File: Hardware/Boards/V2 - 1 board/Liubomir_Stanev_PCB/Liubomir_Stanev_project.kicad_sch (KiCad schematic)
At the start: 16 parts, among them J2 Conn_01x03_Pin, J3 Conn_01x02_Pin, J6 Conn_01x02_Pin, U2 DS18B20-air, U2 DS18B20-water, U4 TEMT6000, U4 Turbidity sensor, U5 GY-8511 UV sensor, U6 Water Level Sensor, U7 ESP32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

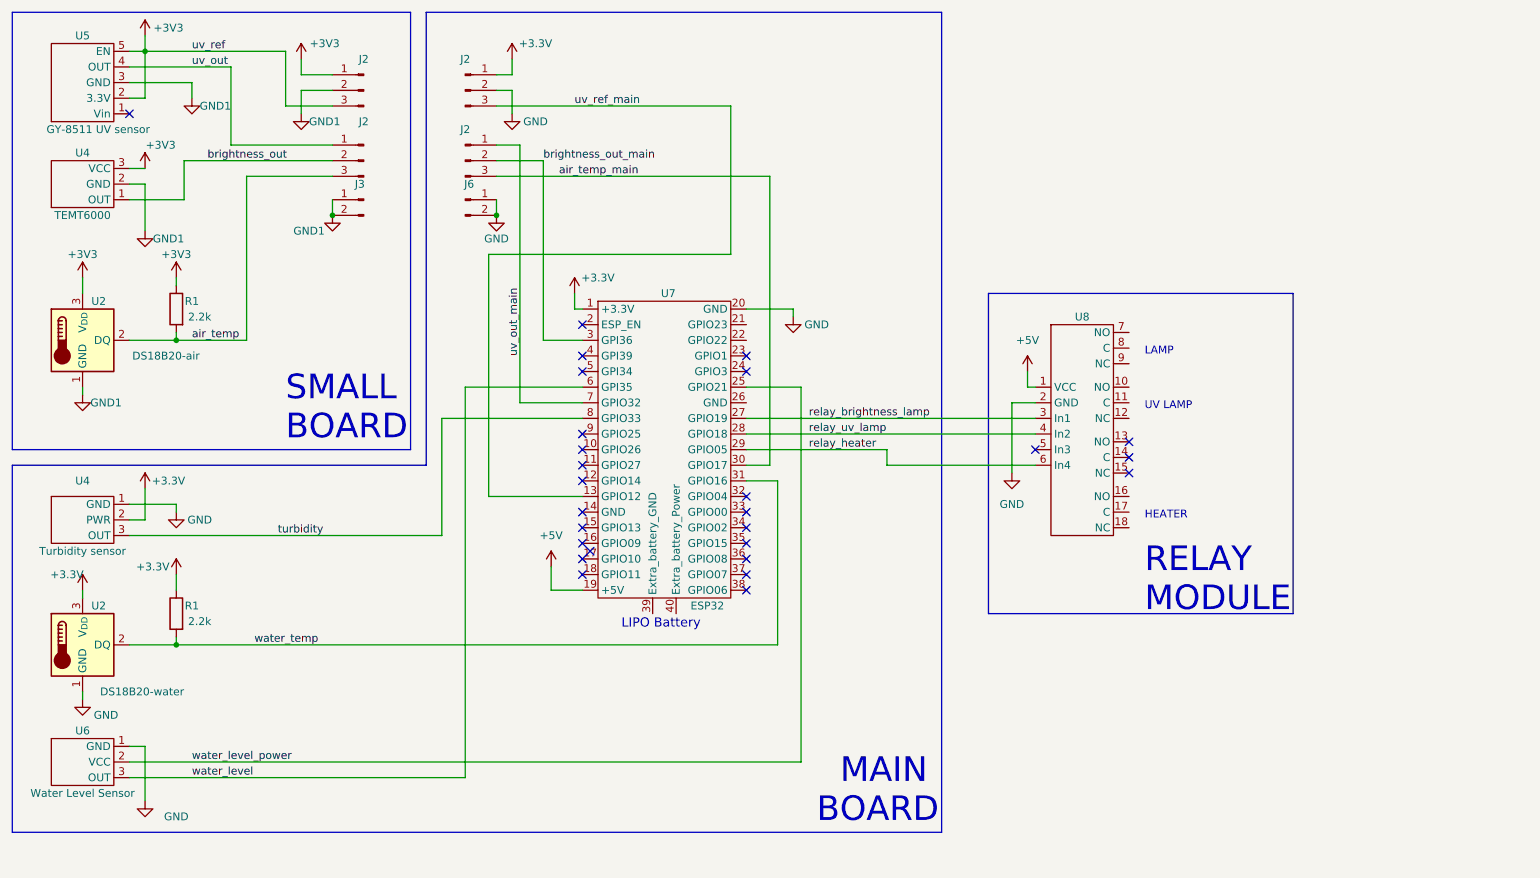
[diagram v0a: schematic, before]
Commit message: Fixed some issues on the board and addded some logic for the turbidity sensor
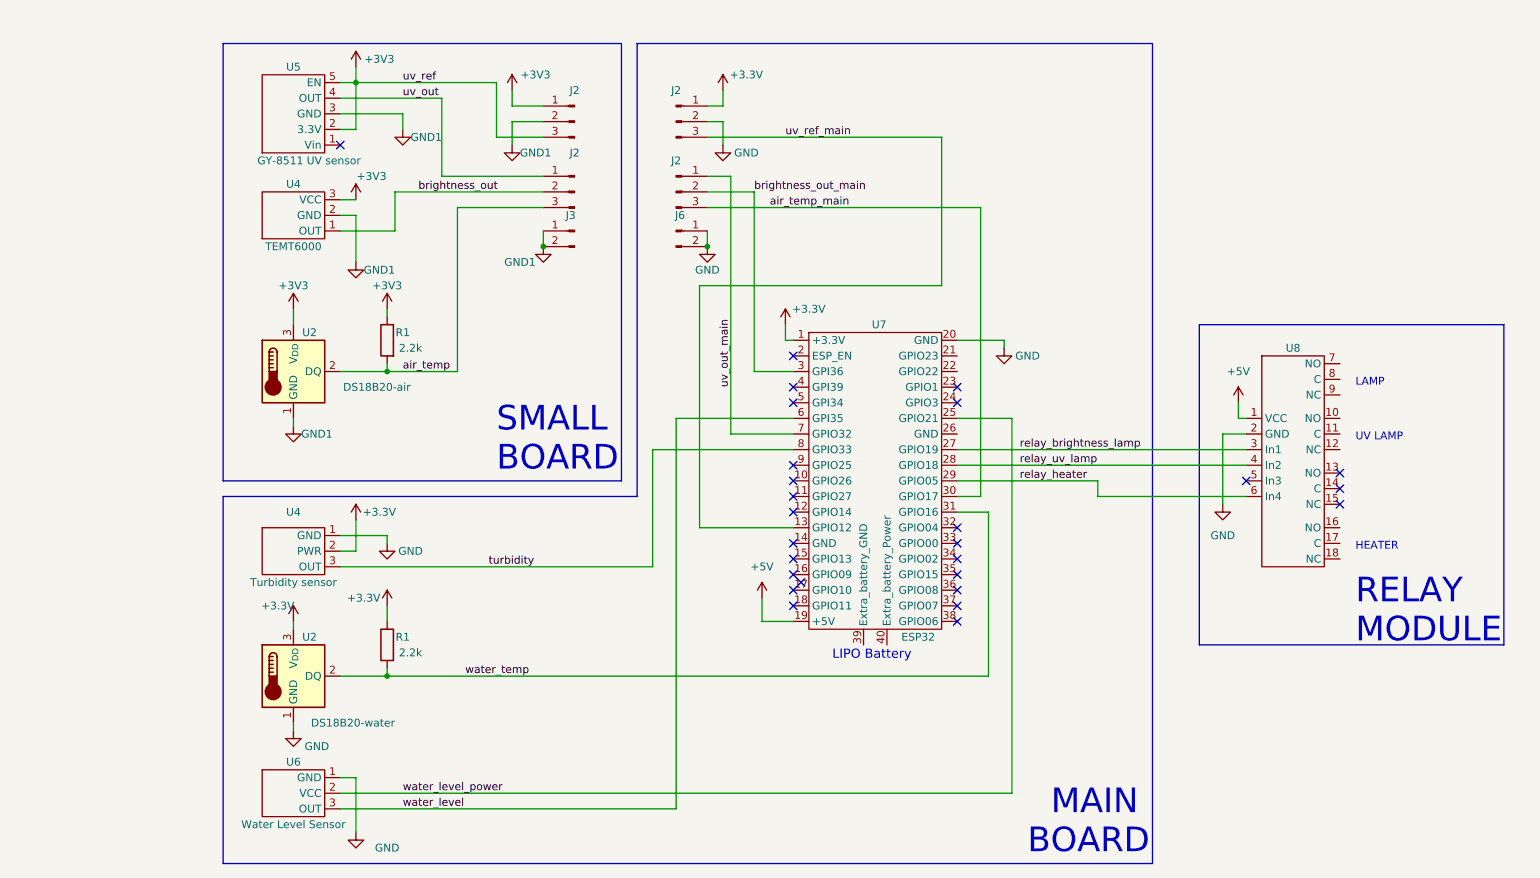
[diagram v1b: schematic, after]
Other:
- moved on the sheet: J2, J3, J6, R1, U2, U4, U5, U6, U7, U8
